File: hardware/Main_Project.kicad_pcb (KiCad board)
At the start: 2 copper layers, 44.5 x 24.8 mm, 1 part

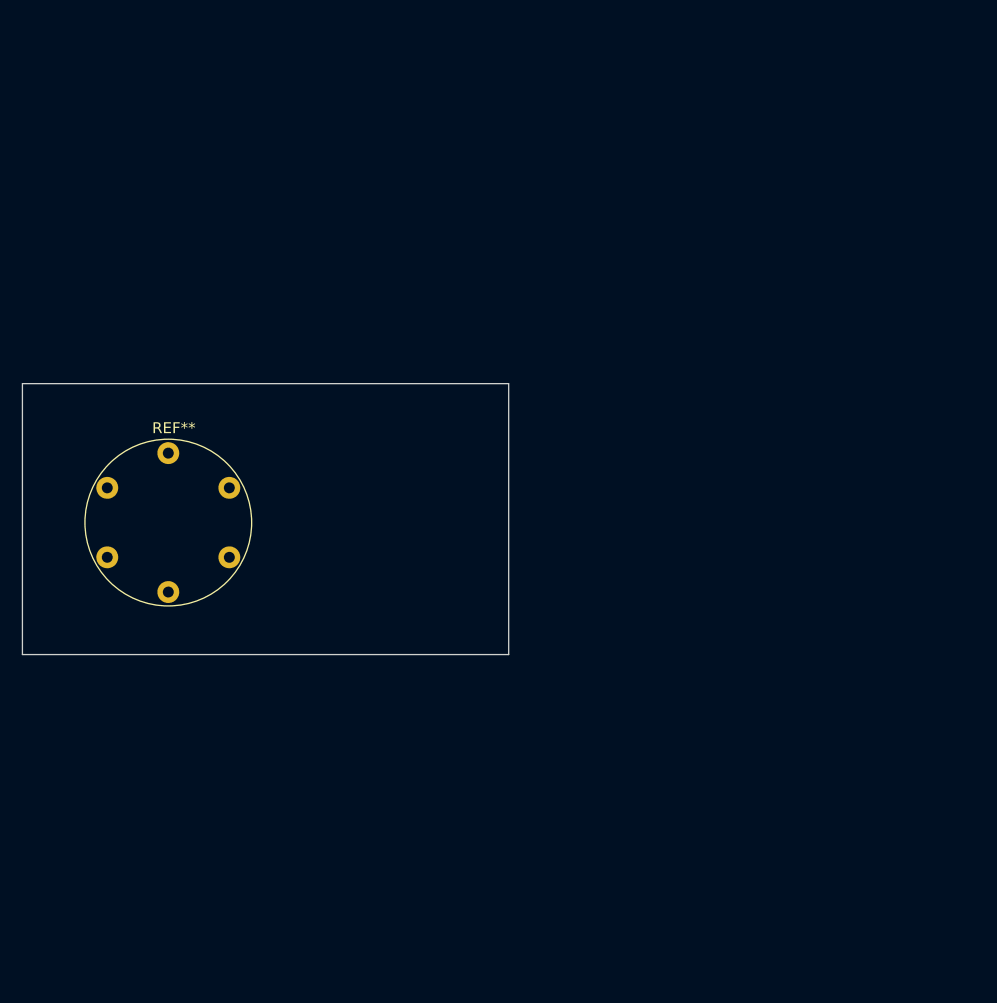
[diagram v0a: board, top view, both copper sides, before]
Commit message: Changed PCB slightly
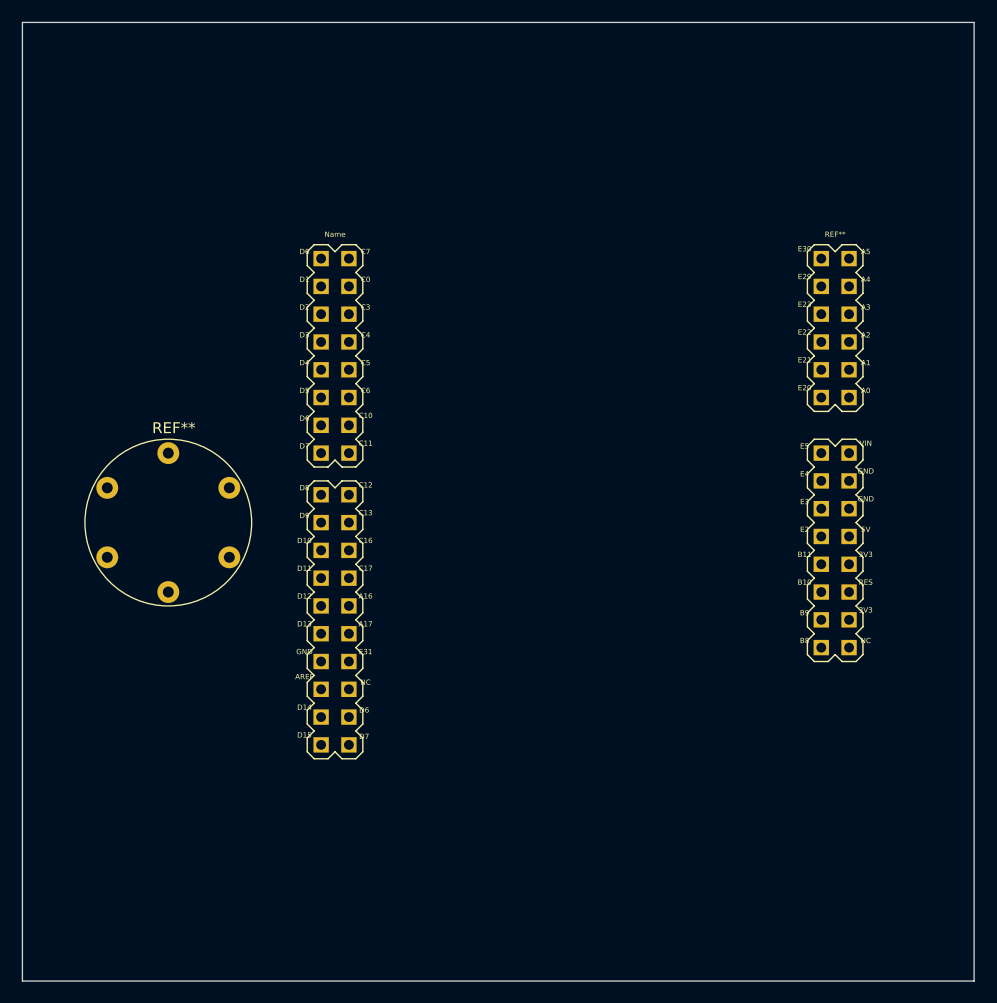
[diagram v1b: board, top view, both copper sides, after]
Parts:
- added REF**: FRDM_KL25Z_NORMAL, TDP3KICAD:FRDM_KL25Z_NORMAL, F.Cu at (203.2, 83.8)
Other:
- board size 44.5 x 24.8 mm -> 87 x 87.6 mm

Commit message: Minor changes
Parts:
- added REFe: Adafruit_Flora_Sensor, TDP3KICAD:Adafruit_Flora_Sensor, F.Cu at (165.1, 106.7)
- renumbered REF** to REFe
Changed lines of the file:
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@@
   )
   (net 0 "")
+  (footprint "TDP3KICAD:Adafruit_Flora_Sensor" (layer "F.Cu")
+    (at 165.1 106.68)
+    (attr through_hole)
+    (fp_text reference "REFe" (at 0.508 -8.636 unlocked) (layer "F.SilkS")
+        (effects (font (size 1 1) (thickness 0.15)))
+    )
+    (fp_text value "Adafruit_Flora_Sensor" (at 0.254 -10.16 unlocked) (layer "F.Fab")
+        (effects (font (size 1 1) (thickness 0.15)))
+    )
+    (fp_circle (center 0 0) (end 7.62 0)
+      (stroke (width 0.12) (type default)) (fill none) (layer "F.SilkS"))
+    (pad "1" thru_hole circle (at 0 -6.35) (size 2.5 2.5) (drill 1.4) (layers "*.Cu" "*.Mask"))
+    (pad "2" thru_hole circle (at -5.58 -3.175) (size 2.5 2.5) (drill 1.4) (layers "*.Cu" "*.Mask"))
+    (pad "3" thru_hole circle (at -5.58 3.175) (size 2.5 2.5) (drill 1.4) (layers "*.Cu" "*.Mask"))
+    (pad "4" thru_hole circle (at 0 6.35) (size 2.5 2.5) (drill 1.4) (layers "*.Cu" "*.Mask"))
+    (pad "5" thru_hole circle (at 5.58 3.175) (size 2.5 2.5) (drill 1.4) (layers "*.Cu" "*.Mask"))
+    (pad "6" thru_hole circle (at 5.58 -3.175) (size 2.5 2.5) (drill 1.4) (layers "*.Cu" "*.Mask"))
+    (model ":MYLIBRARIESMOD:TDP3.pretty/Adafruit Flora TCS34725.step" hide
+      (offset (xyz -148.5 105 3.5))
+      (scale (xyz 1 1 1))
+      (rotate (xyz 0 0 0))
+    )
+    (model ":MYLIBRARIESMOD:TDP3.pretty/flora uv sensor v6.step"
+      (offset (xyz 0 0 0))
+      (scale (xyz 0.87 0.87 0.9))
+      (rotate (xyz 0 0 90))
+    )
+  )
   (footprint "TDP3KICAD:FRDM_KL25Z_NORMAL" (layer "F.Cu")
     (at 203.2 83.82)
@@
     (fp_line (start 26.4 -29.2) (end 26.4 37)
       (stroke (width 0.127) (type solid)) (layer "F.Fab"))
-    (fp_arc (start -26.4 -28.8) (mid -24.069771 -34.727634) (end -18.2 -37.2)
-      (stroke (width 0.127) (type solid)) (layer "F.Fab"))
-    (fp_arc (start -18 45.4) (mid -23.927634 43.069771) (end -26.4 37.2)
-      (stroke (width 0.127) (type solid)) (layer "F.Fab"))
-    (fp_arc (start 18 -37.2) (mid 23.927634 -34.869771) (end 26.4 -29)
-      (stroke (width 0.127) (type solid)) (layer "F.Fab"))
-    (fp_arc (start 26.4 37) (mid 24.069771 42.927634) (end 18.2 45.4)
+    (fp_arc (start -26.4 -28.8) (mid -24.069771 -34.727633) (end -18.2 -37.2)
+      (stroke (width 0.127) (type solid)) (layer "F.Fab"))
+    (fp_arc (start -18 45.4) (mid -23.927633 43.069771) (end -26.4 37.2)
+      (stroke (width 0.127) (type solid)) (layer "F.Fab"))
+    (fp_arc (start 18 -37.2) (mid 23.927633 -34.869771) (end 26.4 -29)
+      (stroke (width 0.127) (type solid)) (layer "F.Fab"))
+    (fp_arc (start 26.4 37) (mid 24.069771 42.927633) (end 18.2 45.4)
       (stroke (width 0.127) (type solid)) (layer "F.Fab"))
     (pad "3V3" thru_hole rect (at 24.13 15.24) (size 1.408 1.408) (drill 0.9) (layers "*.Cu" "*.Mask")
@@
     (at 165.1 90.17)
     (attr through_hole)
-    (fp_text reference "REF**" (at 0.508 -8.636 unlocked) (layer "F.SilkS")
+    (fp_text reference "REFe" (at 0.508 -8.636 unlocked) (layer "F.SilkS")
         (effects (font (size 1 1) (thickness 0.15)))
     )
@@
     (fp_circle (center 0 0) (end 7.62 0)
       (stroke (width 0.12) (type default)) (fill none) (layer "F.SilkS"))
-    (pad "1" thru_hole circle (at 0 -6.35) (size 2 2) (drill 1) (layers "*.Cu" "*.Mask"))
-    (pad "2" thru_hole circle (at -5.58 -3.175) (size 2 2) (drill 1) (layers "*.Cu" "*.Mask"))
-    (pad "3" thru_hole circle (at -5.58 3.175) (size 2 2) (drill 1) (layers "*.Cu" "*.Mask"))
-    (pad "4" thru_hole circle (at 0 6.35) (size 2 2) (drill 1) (layers "*.Cu" "*.Mask"))
-    (pad "5" thru_hole circle (at 5.58 3.175) (size 2 2) (drill 1) (layers "*.Cu" "*.Mask"))
-    (pad "6" thru_hole circle (at 5.58 -3.175) (size 2 2) (drill 1) (layers "*.Cu" "*.Mask"))
+    (pad "1" thru_hole circle (at 0 -6.35) (size 2.5 2.5) (drill 1.4) (layers "*.Cu" "*.Mask"))
+    (pad "2" thru_hole circle (at -5.58 -3.175) (size 2.5 2.5) (drill 1.4) (layers "*.Cu" "*.Mask"))
+    (pad "3" thru_hole circle (at -5.58 3.175) (size 2.5 2.5) (drill 1.4) (layers "*.Cu" "*.Mask"))
+    (pad "4" thru_hole circle (at 0 6.35) (size 2.5 2.5) (drill 1.4) (layers "*.Cu" "*.Mask"))
+    (pad "5" thru_hole circle (at 5.58 3.175) (size 2.5 2.5) (drill 1.4) (layers "*.Cu" "*.Mask"))
+    (pad "6" thru_hole circle (at 5.58 -3.175) (size 2.5 2.5) (drill 1.4) (layers "*.Cu" "*.Mask"))
+    (model ":MYLIBRARIESMOD:TDP3.pretty/Adafruit Flora TCS34725.step" hide
+      (offset (xyz -148.5 105 3.5))
+      (scale (xyz 1 1 1))
+      (rotate (xyz 0 0 0))
+    )
+    (model ":MYLIBRARIESMOD:TDP3.pretty/flora uv sensor v6.step"
+      (offset (xyz 0 0 0))
+      (scale (xyz 0.87 0.87 0.9))
+      (rotate (xyz 0 0 90))
+    )
   )
   (gr_rect (start 151.765 44.45) (end 238.76 132.08)

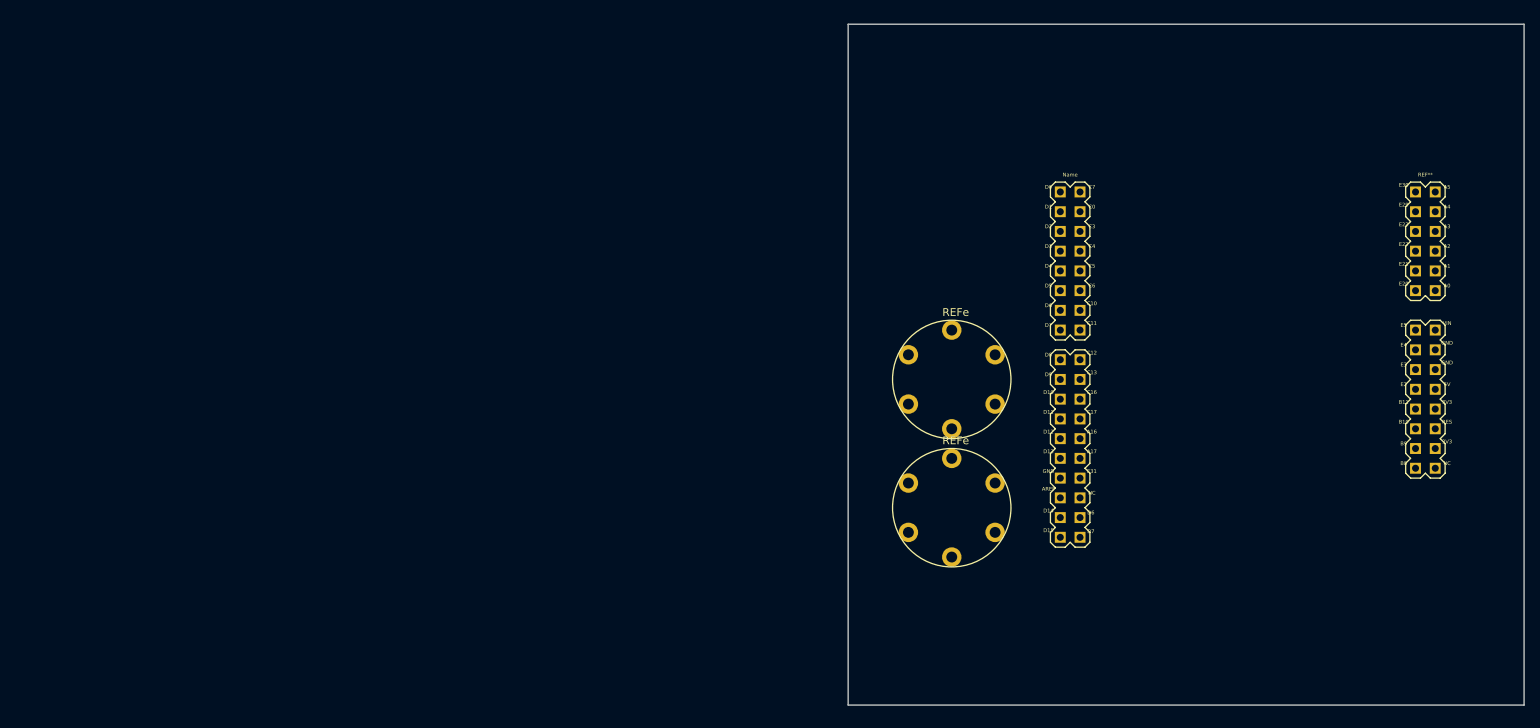
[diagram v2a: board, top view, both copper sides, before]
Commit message: Created Power PCB
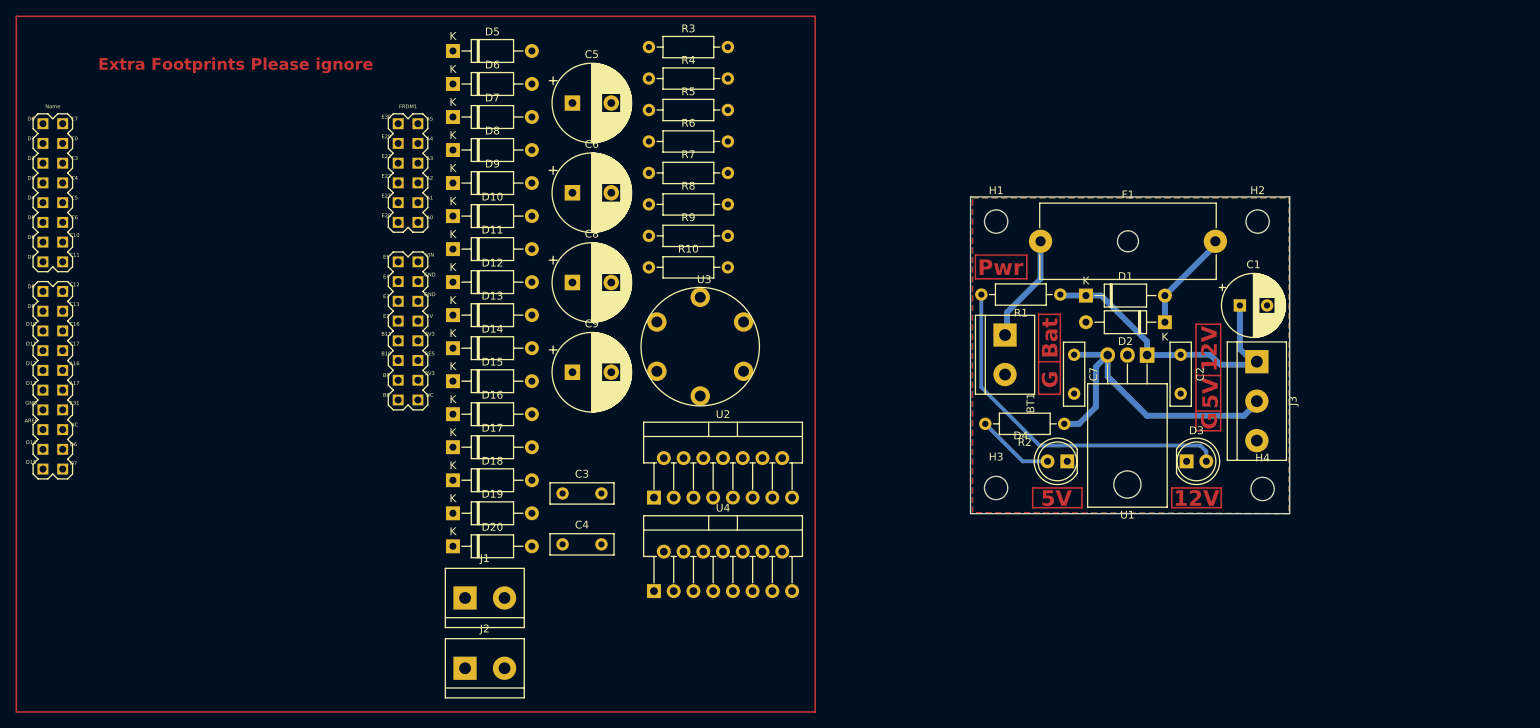
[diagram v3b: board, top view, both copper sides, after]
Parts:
- removed REF**: FRDM_KL25Z_NORMAL, TDP3KICAD:FRDM_KL25Z_NORMAL
- removed REFe (x2): Adafruit_Flora_Sensor, TDP3KICAD:Adafruit_Flora_Sensor
- added BT1: 12V Battery, TerminalBlock:TerminalBlock_bornier-2_P5.08mm, F.Cu at (172.0, 84.5)
- added C1: 4.7uF, Capacitor_THT:CP_Radial_D8.0mm_P3.50mm, F.Cu at (202.2, 80.6)
- added C2: 330nF, Capacitor_THT:C_Disc_D8.0mm_W2.5mm_P5.00mm, F.Cu at (194.6, 87.0)
- added C3: 100nF, Capacitor_THT:C_Disc_D8.0mm_W2.5mm_P5.00mm, F.Cu at (115.0, 104.8)
- added C4: 100nF, Capacitor_THT:C_Disc_D8.0mm_W2.5mm_P5.00mm, F.Cu at (115.0, 111.4)
- added C5: 4.7uF, Capacitor_THT:CP_Radial_D10.0mm_P5.00mm, F.Cu at (116.3, 54.6)
- added C6: 4.7uF, Capacitor_THT:CP_Radial_D10.0mm_P5.00mm, F.Cu at (116.3, 66.1)
- added C7: 100nF, Capacitor_THT:C_Disc_D8.0mm_W2.5mm_P5.00mm, F.Cu at (180.8, 87.0)
- added C8: 4.7uF, Capacitor_THT:CP_Radial_D10.0mm_P5.00mm, F.Cu at (116.3, 77.7)
- added C9: 4.7uF, Capacitor_THT:CP_Radial_D10.0mm_P5.00mm, F.Cu at (116.3, 89.2)
- added D1: 1N4004, Diode_THT:D_A-405_P10.16mm_Horizontal, F.Cu at (182.4, 79.4)
- added D10: D, Diode_THT:D_A-405_P10.16mm_Horizontal, F.Cu at (100.9, 69.1)
- added D11: D, Diode_THT:D_A-405_P10.16mm_Horizontal, F.Cu at (100.9, 73.4)
- added D12: D, Diode_THT:D_A-405_P10.16mm_Horizontal, F.Cu at (100.9, 77.6)
- added D13: D, Diode_THT:D_A-405_P10.16mm_Horizontal, F.Cu at (100.9, 81.9)
- added D14: D, Diode_THT:D_A-405_P10.16mm_Horizontal, F.Cu at (100.9, 86.1)
- added D15: D, Diode_THT:D_A-405_P10.16mm_Horizontal, F.Cu at (100.9, 90.4)
- added D16: D, Diode_THT:D_A-405_P10.16mm_Horizontal, F.Cu at (100.9, 94.6)
- added D17: D, Diode_THT:D_A-405_P10.16mm_Horizontal, F.Cu at (100.9, 98.9)
- added D18: D, Diode_THT:D_A-405_P10.16mm_Horizontal, F.Cu at (100.9, 103.1)
- added D19: D, Diode_THT:D_A-405_P10.16mm_Horizontal, F.Cu at (100.9, 107.4)
- added D2: D_Zener, Diode_THT:D_A-405_P10.16mm_Horizontal, F.Cu at (192.5, 82.8)
- added D20: D, Diode_THT:D_A-405_P10.16mm_Horizontal, F.Cu at (100.9, 111.6)
- added D3: LED_Red, LED_THT:LED_D5.0mm, F.Cu at (195.3, 100.7)
- added D4: LED_Yellow, LED_THT:LED_D5.0mm, F.Cu at (180.0, 100.7)
- added D5: D, Diode_THT:D_A-405_P10.16mm_Horizontal, F.Cu at (100.9, 47.9)
- added D6: D, Diode_THT:D_A-405_P10.16mm_Horizontal, F.Cu at (100.9, 52.1)
- added D7: D, Diode_THT:D_A-405_P10.16mm_Horizontal, F.Cu at (100.9, 56.4)
- added D8: D, Diode_THT:D_A-405_P10.16mm_Horizontal, F.Cu at (100.9, 60.6)
- added D9: D, Diode_THT:D_A-405_P10.16mm_Horizontal, F.Cu at (100.9, 64.9)
- added F1: Fuse, Fuse:Fuseholder_Cylinder-5x20mm_Schurter_0031_8201_Horizontal_Open, F.Cu at (176.5, 72.4)
- added FRDM1: FRDM-KL25Z, TDP3KICAD:FRDM_KL25Z_NORMAL, F.Cu at (72.3, 75.0)
- added H1: MountingHole, MountingHole:MountingHole_3mm, F.Cu at (170.8, 69.8)
- added H2: MountingHole, MountingHole:MountingHole_3mm, F.Cu at (204.5, 69.8)
- added H3: MountingHole, MountingHole:MountingHole_3mm, F.Cu at (170.8, 104.1)
- added H4: MountingHole, MountingHole:MountingHole_3mm, F.Cu at (205.1, 104.3)
- added J1: A_Motor, TerminalBlock:TerminalBlock_bornier-2_P5.08mm, F.Cu at (102.5, 118.3)
- added J2: B_Motor, TerminalBlock:TerminalBlock_bornier-2_P5.08mm, F.Cu at (102.5, 127.3)
- added J3: Power_Outputs, TerminalBlock:TerminalBlock_bornier-3_P5.08mm, F.Cu at (204.4, 87.9)
- added R1: 470R, Resistor_THT:R_Axial_DIN0207_L6.3mm_D2.5mm_P10.16mm_Horizontal, F.Cu at (179.1, 79.2)
- added R10: 1k, Resistor_THT:R_Axial_DIN0207_L6.3mm_D2.5mm_P10.16mm_Horizontal, F.Cu at (126.1, 75.7)
- added R2: 470R, Resistor_THT:R_Axial_DIN0207_L6.3mm_D2.5mm_P10.16mm_Horizontal, F.Cu at (179.6, 95.9)
- added R3: 10k, Resistor_THT:R_Axial_DIN0207_L6.3mm_D2.5mm_P10.16mm_Horizontal, F.Cu at (126.1, 47.4)
- added R4: 10k, Resistor_THT:R_Axial_DIN0207_L6.3mm_D2.5mm_P10.16mm_Horizontal, F.Cu at (126.1, 51.4)
- added R5: 1k, Resistor_THT:R_Axial_DIN0207_L6.3mm_D2.5mm_P10.16mm_Horizontal, F.Cu at (126.1, 55.5)
- added R6: 1k, Resistor_THT:R_Axial_DIN0207_L6.3mm_D2.5mm_P10.16mm_Horizontal, F.Cu at (126.1, 59.5)
- added R7: 10k, Resistor_THT:R_Axial_DIN0207_L6.3mm_D2.5mm_P10.16mm_Horizontal, F.Cu at (126.1, 63.6)
- added R8: 10k, Resistor_THT:R_Axial_DIN0207_L6.3mm_D2.5mm_P10.16mm_Horizontal, F.Cu at (126.1, 67.6)
- added R9: 1k, Resistor_THT:R_Axial_DIN0207_L6.3mm_D2.5mm_P10.16mm_Horizontal, F.Cu at (126.1, 71.7)
- added U1: L7805, Package_TO_SOT_THT:TO-220-3_Horizontal_TabDown, F.Cu at (190.2, 87.0)
- added U2: L298N, Package_TO_SOT_THT:TO-220-15_P2.54x2.54mm_StaggerOdd_Lead4.58mm_Vertical, F.Cu at (126.8, 105.4)
- added U3: ~, TDP3KICAD:Adafruit_Flora_Sensor, F.Cu at (132.7, 85.9)
- added U4: L298N, Package_TO_SOT_THT:TO-220-15_P2.54x2.54mm_StaggerOdd_Lead4.58mm_Vertical, F.Cu at (126.8, 117.4)
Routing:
- net Net-(D3-A): track 0.00 -> 45.6 mm
- net +5V: track 0.00 -> 41.1 mm
- net +12V: track 0.00 -> 38.4 mm
- net Net-(BT1-+): track 0.00 -> 13.9 mm
- net Net-(D1-A): track 0.00 -> 13.1 mm
- net Net-(D4-A): track 0.00 -> 10.0 mm
- added copper zone on B.Cu, net GND
- added copper zone on F.Cu, net GND
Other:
- board size 87 x 87.6 mm -> 41.1 x 40.8 mm
- board text added: "12V"
- board text added: "5V"
- board text added: "Bat"
- board text added: "Extra Footprints Please ignore"
- board text added: "G"
- board text added: "Pwr"

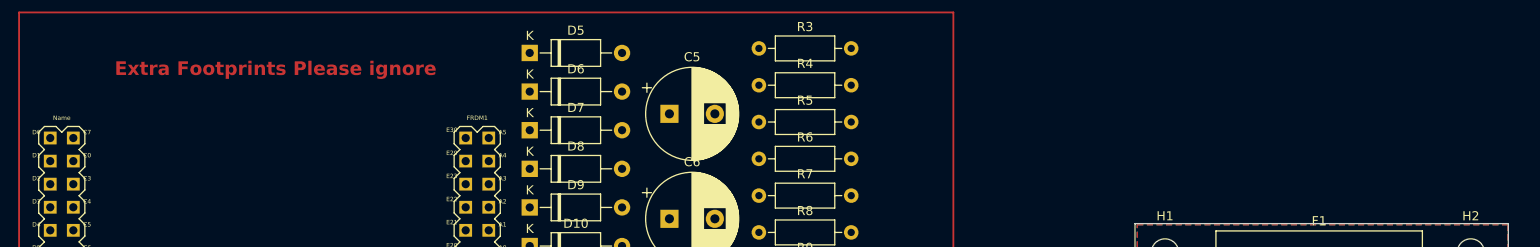
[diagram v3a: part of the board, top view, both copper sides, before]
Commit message: Created photomasks folder and made photomasks for power PCB
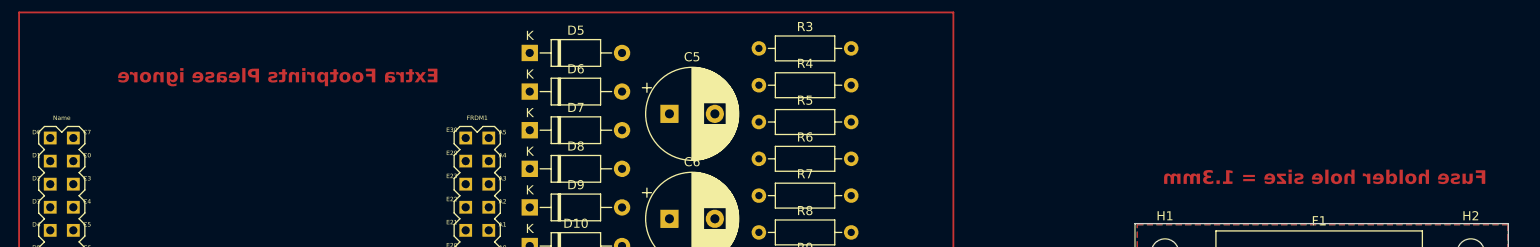
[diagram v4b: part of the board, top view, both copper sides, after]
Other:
- board text added: "Fuse holder hole size = 1.3mm"
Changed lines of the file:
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@@
   (gr_rect (start 167.513 66.675) (end 208.5975 107.442)
     (stroke (width 0.1) (type default)) (fill none) (layer "Edge.Cuts"))
+  (gr_text "Fuse holder hole size = 1.3mm" (at 206.248 62.484) (layer "F.Cu")
+    (effects (font (size 1.5 1.5) (thickness 0.3) bold) (justify left bottom mirror))
+  )
   (gr_text "12V\n" (at 199.4535 86.233 90) (layer "F.Cu")
     (effects (font (face "Nunito Black") (size 2 2) (thickness 0.3) bold) (justify bottom))
@@
     )
   )
-  (gr_text "Extra Footprints Please ignore" (at 55.2196 50.4952) (layer "F.Cu")
-    (effects (font (size 1.5 1.5) (thickness 0.3) bold) (justify left bottom))
+  (gr_text "Extra Footprints Please ignore" (at 90.932 51.308) (layer "F.Cu")
+    (effects (font (size 1.5 1.5) (thickness 0.3) bold) (justify left bottom mirror))
   )
   (gr_text "Bat" (at 178.943 84.836 90) (layer "F.Cu")
